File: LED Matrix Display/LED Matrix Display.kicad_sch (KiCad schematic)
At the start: 5 parts, among them J1 I2C Sensor 1, J2 LED Display

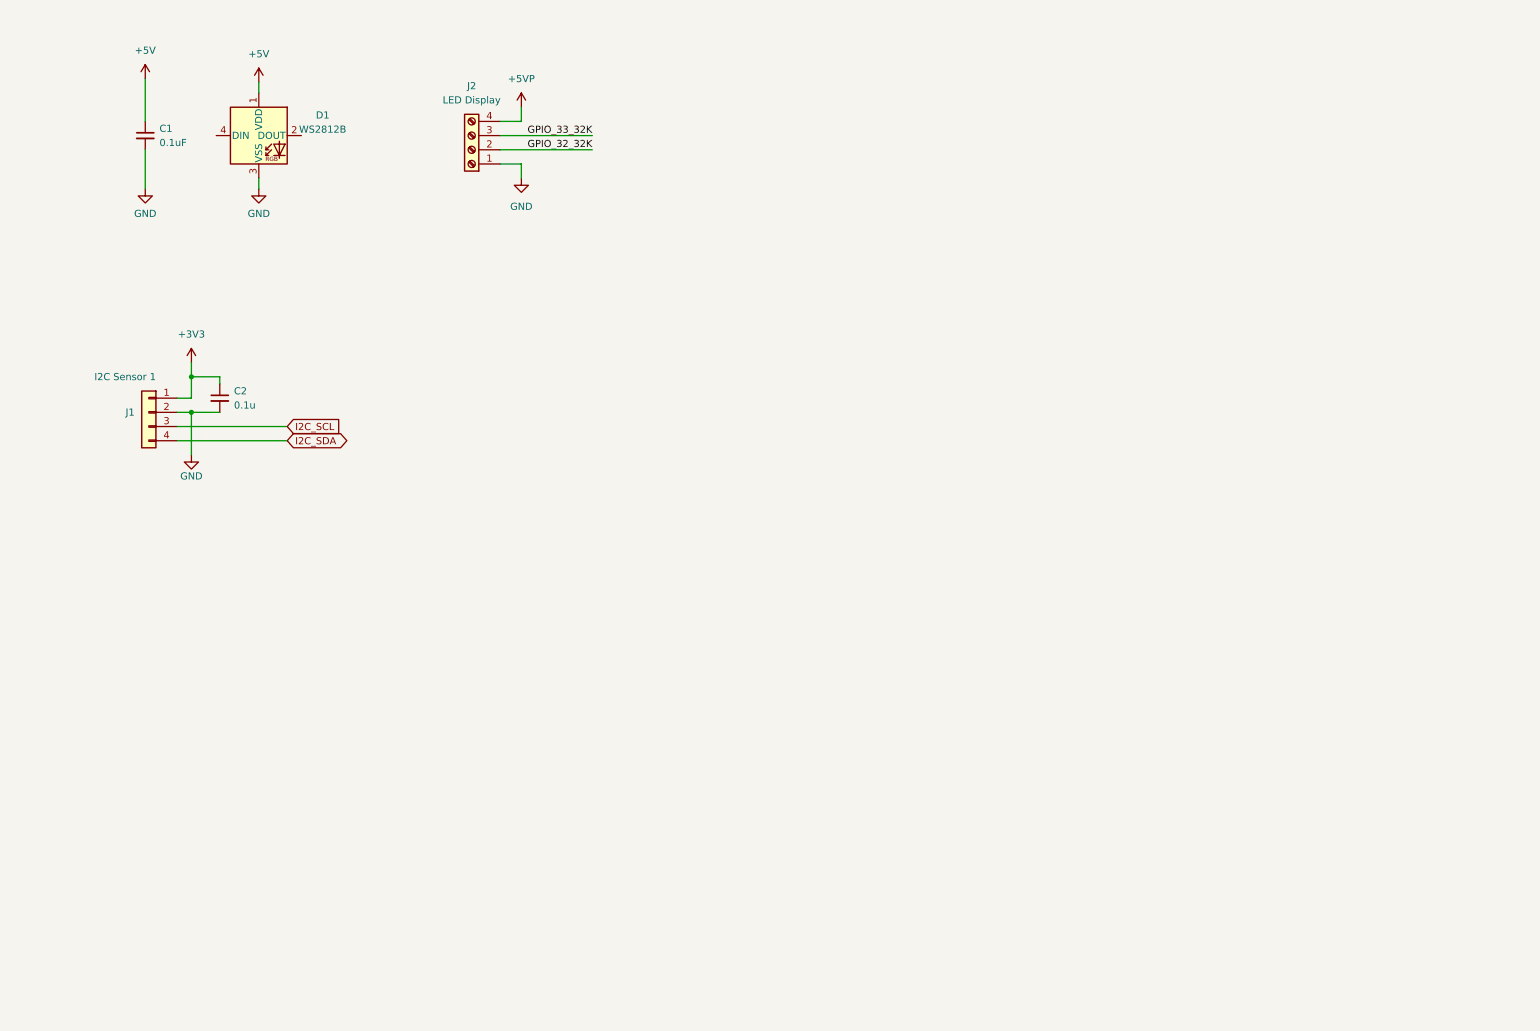
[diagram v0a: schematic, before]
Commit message: added esp32
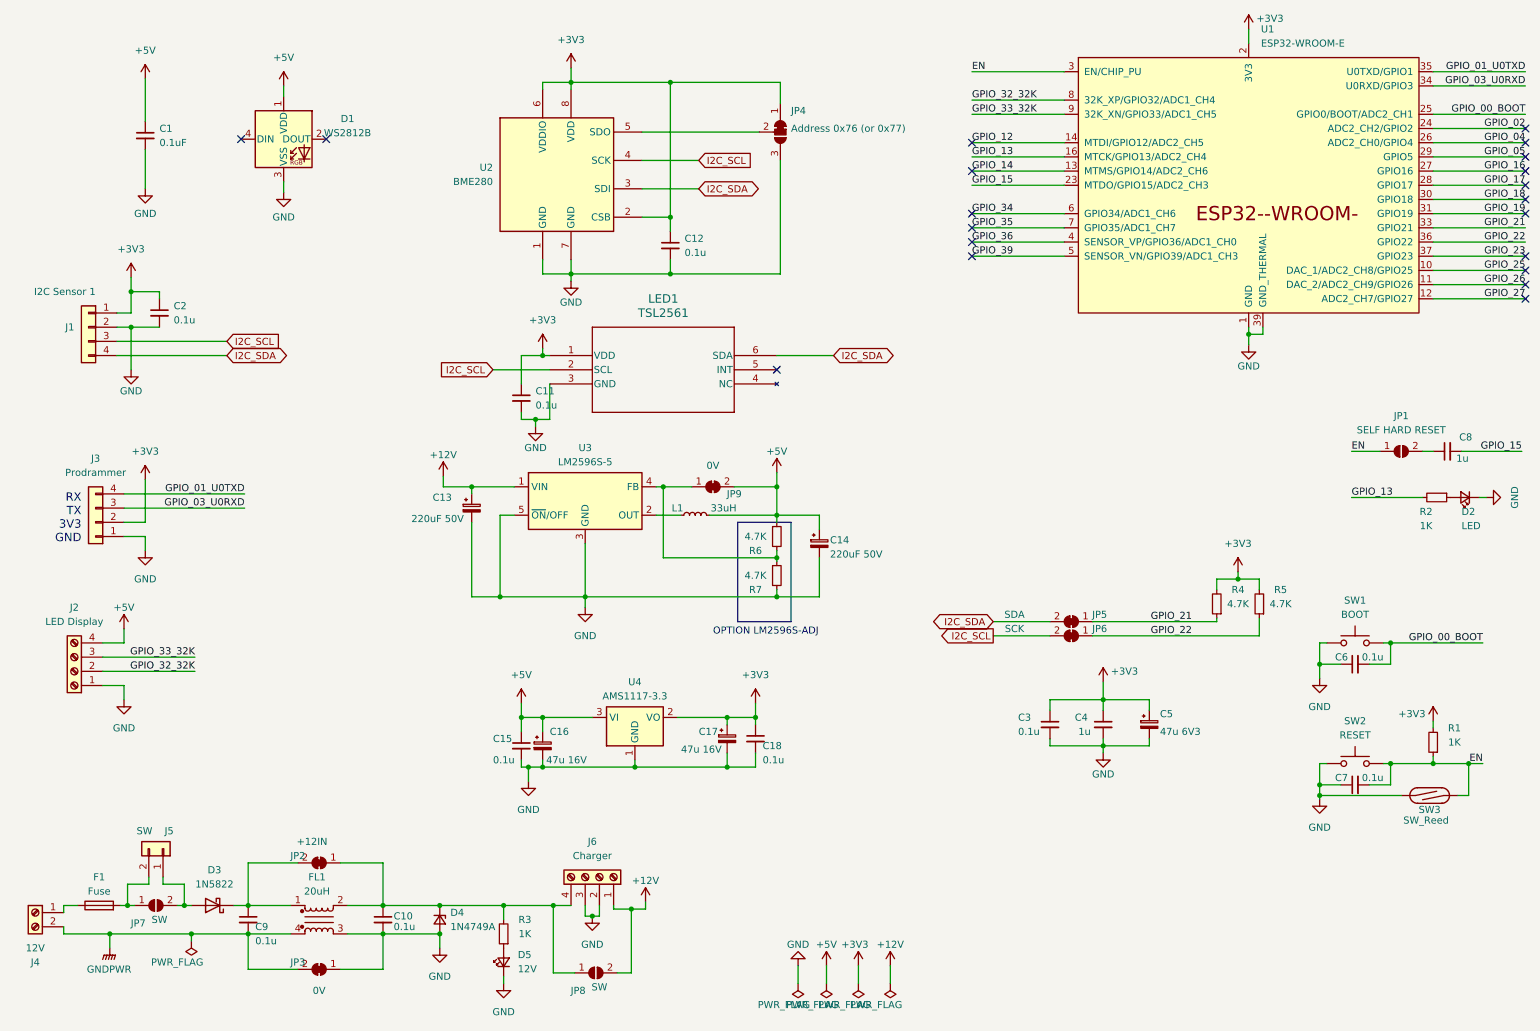
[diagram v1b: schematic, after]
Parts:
- added C10, C11, C12, C15, C18, C3, C6, C7, C9: 0.1u, Capacitor_SMD:C_0805_2012Metric_Pad1.18x1.45mm_HandSolder, symbol Device:C_Small
- added C13, C14: 220uF 50V, Capacitor_SMD:CP_Elec_5x5.8, symbol Device:C_Polarized_Small
- added C16, C17: 47u 16V, Capacitor_SMD:CP_Elec_5x5.8, symbol Device:C_Polarized_Small
- added C4, C8: 1u, Capacitor_SMD:C_0805_2012Metric_Pad1.18x1.45mm_HandSolder, symbol Device:C_Small
- added C5: 47u 6V3, Capacitor_Tantalum_SMD:CP_EIA-3528-21_Kemet-B_Pad1.50x2.35mm_HandSolder, symbol Device:C_Polarized_Small
- added D2: LED, LED_SMD:LED_0805_2012Metric_Pad1.15x1.40mm_HandSolder, symbol Device:LED_Small
- added D3: 1N5822, Diode_SMD:D_SMC, symbol Diode:1N5822
- added D4: 1N4749A, Diode_SMD:D_SMA, symbol Device:D_Zener_Small
- added D5: 12V, LED_SMD:LED_0805_2012Metric_Pad1.15x1.40mm_HandSolder, symbol Device:LED_Small
- added F1: Fuse, Fuse:Fuse_1812_4532Metric, symbol Device:Fuse
- added FL1: 20uH, Transformer_SMD:Pulse_PA2001NL, symbol Device:Filter_EMI_CommonMode
- added J3: Prodrammer, Connector_JST:JST_PH_S4B-PH-SM4-TB_1x04-1MP_P2.00mm_Horizontal, symbol Connector_Generic:Conn_01x04
- added J4: 12V, Connector_Molex:Molex_Micro-Fit_3.0_43650-0210_1x02-1MP_P3.00mm_Horizontal_PnP, symbol Connector:Screw_Terminal_01x02
- added J5: SW, Connector_Molex:Molex_Micro-Fit_3.0_43650-0210_1x02-1MP_P3.00mm_Horizontal_PnP, symbol Connector_Generic:Conn_01x02
- added J6: Charger, Connector_Molex:Molex_Micro-Fit_3.0_43650-0410_1x04-1MP_P3.00mm_Horizontal_PnP, symbol Connector:Screw_Terminal_01x04
- added JP1: SELF HARD RESET, Jumper:SolderJumper-2_P1.3mm_Open_RoundedPad1.0x1.5mm, symbol Jumper:SolderJumper_2_Open
- added JP2: +12IN, 1Display:NOSILK SolderJumper-2_P1.3mm_Open_Pad1.0x1.5mm, symbol Jumper:SolderJumper_2_Bridged
- added JP3, JP9: 0V, 1Display:NOSILK SolderJumper-2_P1.3mm_Open_Pad1.0x1.5mm, symbol Jumper:SolderJumper_2_Bridged
- added JP4: Address 0x76 (or 0x77), Jumper:SolderJumper-3_P1.3mm_Bridged12_Pad1.0x1.5mm, symbol Jumper:SolderJumper_3_Bridged12
- added JP5: SDA, Jumper:SolderJumper-2_P1.3mm_Bridged_Pad1.0x1.5mm, symbol Jumper:SolderJumper_2_Bridged
- added JP6: SCK, Jumper:SolderJumper-2_P1.3mm_Bridged_Pad1.0x1.5mm, symbol Jumper:SolderJumper_2_Bridged
- added JP7, JP8: SW, Jumper:SolderJumper-2_P1.3mm_Open_RoundedPad1.0x1.5mm, symbol Jumper:SolderJumper_2_Open
- added L1: 33uH, Inductor_SMD:L_12x12mm_H4.5mm, symbol Device:L_Small
- added LED1: TSL2561, 1Display:TSL2561, symbol 1Display2:TSL25723FN
- added R1, R2, R3: 1K, Resistor_SMD:R_0805_2012Metric_Pad1.20x1.40mm_HandSolder, symbol Device:R_Small
- added R4, R5, R6, R7: 4.7K, Resistor_SMD:R_0805_2012Metric_Pad1.20x1.40mm_HandSolder, symbol Device:R_Small
- added SW1: BOOT, Button_Switch_SMD:SW_Push_1P1T_NO_6x6mm_H9.5mm, symbol Switch:SW_Push
- added SW2: RESET, Button_Switch_SMD:SW_Push_1P1T_NO_6x6mm_H9.5mm, symbol Switch:SW_Push
- added SW3: SW_Reed, Button_Switch_SMD:SW_SPST_REED_CT05-XXXX-J1, symbol Switch:SW_Reed
- added U1: ESP32-WROOM-E, PCM_Espressif:ESP32-WROOM-32E, symbol PCM_Espressif:ESP32-WROOM-E
- added U2: BME280, Package_LGA:Bosch_LGA-8_2.5x2.5mm_P0.65mm_ClockwisePinNumbering, symbol Sensor:BME280
- added U3: LM2596S-5, Package_TO_SOT_SMD:TO-263-5_TabPin3, symbol Regulator_Switching:LM2596S-5
- added U4: AMS1117-3.3, Package_TO_SOT_SMD:SOT-223-3_TabPin2, symbol Regulator_Linear:AMS1117-5.0
- J1: footprint Connector_JST:JST_PH_B4B-PH-SM4-TB_1x04-1MP_P2.00mm_Vertical -> Connector_JST:JST_PH_S4B-PH-SM4-TB_1x04-1MP_P2.00mm_Horizontal
- J2: footprint Connector_Molex:Molex_Micro-Fit_3.0_43045-0418_2x02-1MP_P3.00mm_Vertical -> Connector_Molex:Molex_Micro-Fit_3.0_43650-0410_1x04-1MP_P3.00mm_Horizontal_PnP
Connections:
- net +5VP is gone; now on net +5V: J2.4 (Pin_4)
- net +3V3: now also C11.1, C12.1, C17.1, C18.1, C3.1, C4.1, C5.1, J3.2 (Pin_2), JP4.1 (A), LED1.1 (VDD), R1.2, R4.2, R5.2, U1.2 (3V3), U2.2 (CSB), U2.6 (VDDIO), U2.8 (VDD), U4.2 (VO)
- net +5V: now also C14.1, C15.1, C16.1, JP9.2 (B), L1.2, R6.1, U4.3 (VI)
- net GND: now also C10.2, C11.2, C12.2, C13.2, C14.2, C15.2, C16.2, C17.2, C18.2, C3.2, C4.2, C5.2, C6.1, C7.1, D2.1 (K), D4.2 (A), D5.1 (K), FL1.3, J3.1 (Pin_1), J6.2 (Pin_2), J6.3 (Pin_3), JP3.1 (A), JP4.3 (B), LED1.3 (GND), R7.2, SW1.1, SW2.1, SW3.1, U1.1 (GND), U1.15 (GND), U1.38 (GND), U1.39 (GND_THERMAL), U2.1 (GND), U2.7 (GND), U3.3 (GND), U3.5 (~{ON}/OFF), U4.1 (GND)
- net GPIO_32_32K: now also U1.8 (32K_XP/GPIO32/ADC1_CH4)
- net GPIO_33_32K: now also U1.9 (32K_XN/GPIO33/ADC1_CH5)
- net I2C_SCL: now also JP6.2 (B), LED1.2 (SCL), U2.4 (SCK)
- net I2C_SDA: now also JP5.2 (B), LED1.6 (SDA), U2.3 (SDI)
- new net: C10.1, D4.1 (K), FL1.2, J6.4 (Pin_4), JP2.1 (A), JP8.1 (A), R3.2
- new net: C9.1, D3.1 (K), FL1.1, JP2.2 (B)
- new net: L1.1, U3.2 (OUT)
- new net: JP9.1 (A), R6.2, R7.1, U3.4 (FB)
- new net: D5.2 (A), R3.1
- new net: C8.1, JP1.2 (B)
- new net: JP4.2 (C), U2.5 (SDO)
- new net: D2.2 (A), R2.1
- new net: F1.2, J5.2 (Pin_2), JP7.1 (A)
- new net: D3.2 (A), J5.1 (Pin_1), JP7.2 (B)
- new net: F1.1, J4.1 (Pin_1)
- new net +12V: C13.1, J6.1 (Pin_1), JP8.2 (B), U3.1 (VIN)
- new net EN: C7.2, JP1.1 (A), R1.1, SW2.2, SW3.2, U1.3 (EN/CHIP_PU)
- new net GNDPWR: C9.2, FL1.4, J4.2 (Pin_2), JP3.2 (B)
- new net GPIO_00_BOOT: C6.2, SW1.2, U1.25 (GPIO0/BOOT/ADC2_CH1)
- new net GPIO_01_U0TXD: J3.4 (Pin_4), U1.35 (U0TXD/GPIO1)
- new net GPIO_02: U1.24 (ADC2_CH2/GPIO2)
- new net GPIO_03_U0RXD: J3.3 (Pin_3), U1.34 (U0RXD/GPIO3)
- new net GPIO_04: U1.26 (ADC2_CH0/GPIO4)
- new net GPIO_05: U1.29 (GPIO5)
- new net GPIO_12: U1.14 (MTDI/GPIO12/ADC2_CH5)
- new net GPIO_13: R2.2, U1.16 (MTCK/GPIO13/ADC2_CH4)
- new net GPIO_14: U1.13 (MTMS/GPIO14/ADC2_CH6)
- new net GPIO_15: C8.2, U1.23 (MTDO/GPIO15/ADC2_CH3)
- new net GPIO_16: U1.27 (GPIO16)
- new net GPIO_17: U1.28 (GPIO17)
- new net GPIO_18: U1.30 (GPIO18)
- new net GPIO_19: U1.31 (GPIO19)
- new net GPIO_21: JP5.1 (A), R4.1, U1.33 (GPIO21)
- new net GPIO_22: JP6.1 (A), R5.1, U1.36 (GPIO22)
- new net GPIO_23: U1.37 (GPIO23)
- new net GPIO_25: U1.10 (DAC_1/ADC2_CH8/GPIO25)
- new net GPIO_26: U1.11 (DAC_2/ADC2_CH9/GPIO26)
- new net GPIO_27: U1.12 (ADC2_CH7/GPIO27)
- new net GPIO_34: U1.6 (GPIO34/ADC1_CH6)
- new net GPIO_35: U1.7 (GPIO35/ADC1_CH7)
- new net GPIO_36: U1.4 (SENSOR_VP/GPIO36/ADC1_CH0)
- new net GPIO_39: U1.5 (SENSOR_VN/GPIO39/ADC1_CH3)
- no-connect marks 0 -> 20
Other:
- note added: "OPTION LM2596S-ADJ"
- note added: "RX TX 3V3 GND"
- moved on the sheet: C2, D1, J1, J2

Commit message: LED
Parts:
- removed C1: 0.1uF, Capacitor_SMD:C_0402_1005Metric, symbol Device:C_Small
- removed C10, C11, C12, C15, C18, C2, C3, C6, C7, C9: 0.1u, Capacitor_SMD:C_0805_2012Metric_Pad1.18x1.45mm_HandSolder, symbol Device:C_Small
- removed C13, C14: 220uF 50V, Capacitor_SMD:CP_Elec_5x5.8, symbol Device:C_Polarized_Small
- removed C16, C17: 47u 16V, Capacitor_SMD:CP_Elec_5x5.8, symbol Device:C_Polarized_Small
- removed C4, C8: 1u, Capacitor_SMD:C_0805_2012Metric_Pad1.18x1.45mm_HandSolder, symbol Device:C_Small
- removed C5: 47u 6V3, Capacitor_Tantalum_SMD:CP_EIA-3528-21_Kemet-B_Pad1.50x2.35mm_HandSolder, symbol Device:C_Polarized_Small
- removed D1: WS2812B, LED_SMD:LED_WS2812B_PLCC4_5.0x5.0mm_P3.2mm, symbol LED:WS2812B
- removed D2: LED, LED_SMD:LED_0805_2012Metric_Pad1.15x1.40mm_HandSolder, symbol Device:LED_Small
- removed D3: 1N5822, Diode_SMD:D_SMC, symbol Diode:1N5822
- removed D4: 1N4749A, Diode_SMD:D_SMA, symbol Device:D_Zener_Small
- removed D5: 12V, LED_SMD:LED_0805_2012Metric_Pad1.15x1.40mm_HandSolder, symbol Device:LED_Small
- removed F1: Fuse, Fuse:Fuse_1812_4532Metric, symbol Device:Fuse
- removed FL1: 20uH, Transformer_SMD:Pulse_PA2001NL, symbol Device:Filter_EMI_CommonMode
- removed J1: I2C Sensor 1, Connector_JST:JST_PH_S4B-PH-SM4-TB_1x04-1MP_P2.00mm_Horizontal, symbol Connector_Generic:Conn_01x04
- removed J2: LED Display, Connector_Molex:Molex_Micro-Fit_3.0_43650-0410_1x04-1MP_P3.00mm_Horizontal_PnP, symbol Connector:Screw_Terminal_01x04
- removed J3: Prodrammer, Connector_JST:JST_PH_S4B-PH-SM4-TB_1x04-1MP_P2.00mm_Horizontal, symbol Connector_Generic:Conn_01x04
- removed J4: 12V, Connector_Molex:Molex_Micro-Fit_3.0_43650-0210_1x02-1MP_P3.00mm_Horizontal_PnP, symbol Connector:Screw_Terminal_01x02
- removed J5: SW, Connector_Molex:Molex_Micro-Fit_3.0_43650-0210_1x02-1MP_P3.00mm_Horizontal_PnP, symbol Connector_Generic:Conn_01x02
- removed J6: Charger, Connector_Molex:Molex_Micro-Fit_3.0_43650-0410_1x04-1MP_P3.00mm_Horizontal_PnP, symbol Connector:Screw_Terminal_01x04
- removed JP1: SELF HARD RESET, Jumper:SolderJumper-2_P1.3mm_Open_RoundedPad1.0x1.5mm, symbol Jumper:SolderJumper_2_Open
- removed JP2: +12IN, 1Display:NOSILK SolderJumper-2_P1.3mm_Open_Pad1.0x1.5mm, symbol Jumper:SolderJumper_2_Bridged
- removed JP3, JP9: 0V, 1Display:NOSILK SolderJumper-2_P1.3mm_Open_Pad1.0x1.5mm, symbol Jumper:SolderJumper_2_Bridged
- removed JP4: Address 0x76 (or 0x77), Jumper:SolderJumper-3_P1.3mm_Bridged12_Pad1.0x1.5mm, symbol Jumper:SolderJumper_3_Bridged12
- removed JP5: SDA, Jumper:SolderJumper-2_P1.3mm_Bridged_Pad1.0x1.5mm, symbol Jumper:SolderJumper_2_Bridged
- removed JP6: SCK, Jumper:SolderJumper-2_P1.3mm_Bridged_Pad1.0x1.5mm, symbol Jumper:SolderJumper_2_Bridged
- removed JP7, JP8: SW, Jumper:SolderJumper-2_P1.3mm_Open_RoundedPad1.0x1.5mm, symbol Jumper:SolderJumper_2_Open
- removed L1: 33uH, Inductor_SMD:L_12x12mm_H4.5mm, symbol Device:L_Small
- removed LED1: TSL2561, 1Display:TSL2561, symbol 1Display2:TSL25723FN
- removed R1, R2, R3: 1K, Resistor_SMD:R_0805_2012Metric_Pad1.20x1.40mm_HandSolder, symbol Device:R_Small
- removed R4, R5, R6, R7: 4.7K, Resistor_SMD:R_0805_2012Metric_Pad1.20x1.40mm_HandSolder, symbol Device:R_Small
- removed SW1: BOOT, Button_Switch_SMD:SW_Push_1P1T_NO_6x6mm_H9.5mm, symbol Switch:SW_Push
- removed SW2: RESET, Button_Switch_SMD:SW_Push_1P1T_NO_6x6mm_H9.5mm, symbol Switch:SW_Push
- removed SW3: SW_Reed, Button_Switch_SMD:SW_SPST_REED_CT05-XXXX-J1, symbol Switch:SW_Reed
- removed U1: ESP32-WROOM-E, PCM_Espressif:ESP32-WROOM-32E, symbol PCM_Espressif:ESP32-WROOM-E
- removed U2: BME280, Package_LGA:Bosch_LGA-8_2.5x2.5mm_P0.65mm_ClockwisePinNumbering, symbol Sensor:BME280
- removed U3: LM2596S-5, Package_TO_SOT_SMD:TO-263-5_TabPin3, symbol Regulator_Switching:LM2596S-5
- removed U4: AMS1117-3.3, Package_TO_SOT_SMD:SOT-223-3_TabPin2, symbol Regulator_Linear:AMS1117-5.0
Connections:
- no-connect marks 20 -> 0
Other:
- added sheet ESP32 (ESP32.kicad_sch)
- added sheet LEDS Only (LEDS Only.kicad_sch)
- note removed: "OPTION LM2596S-ADJ"
- note removed: "RX TX 3V3 GND"

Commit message: LED MX Release candidate
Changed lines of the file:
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@@
 (kicad_sch (version 20230121) (generator eeschema)
   (paper "A4")
-  (sheet (at 149.225 24.13) (size 23.495 19.685) (fields_autoplaced)
+  (sheet (at 149.225 24.13) (size 85.725 80.01) (fields_autoplaced)
     (stroke (width 0.1524) (type solid))
     (fill (color 0 0 0 0.0000))
@@
       (effects (font (size 1.27 1.27)) (justify left bottom))
     )
-    (property "Sheetfile" "ESP32.kicad_sch" (at 149.225 44.3996 0)
+    (property "Sheetfile" "ESP32.kicad_sch" (at 149.225 104.7246 0)
       (effects (font (size 1.27 1.27)) (justify left top))
     )
@@
     )
   )
-  (sheet (at 114.3 24.13) (size 27.305 19.05) (fields_autoplaced)
+  (sheet (at 40.64 24.13) (size 100.965 80.01) (fields_autoplaced)
     (stroke (width 0.1524) (type solid))
     (fill (color 0 0 0 0.0000))
-    (property "Sheetname" "LEDS Only" (at 114.3 23.4184 0)
+    (property "Sheetname" "LEDS Only" (at 40.64 23.4184 0)
       (effects (font (size 1.27 1.27)) (justify left bottom))
     )
-    (property "Sheetfile" "LEDS Only.kicad_sch" (at 114.3 43.7646 0)
+    (property "Sheetfile" "LEDS Only.kicad_sch" (at 40.64 104.7246 0)
       (effects (font (size 1.27 1.27)) (justify left top))
     )
-    (property "Field2" "" (at 114.3 24.13 0)
+    (property "Field2" "" (at 40.64 24.13 0)
       (effects (font (size 1.27 1.27)) hide)
     )
